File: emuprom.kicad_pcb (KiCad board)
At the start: 2 copper layers, 91.4 x 68.6 mm, 34 parts, among them J1 Conn_02x20_Odd_Even, J2 Conn_02x03_Odd_Even, J3 USB_C_Receptacle_USB2.0_14P, J4 Conn_01x02, U1 CY62256-70PC, U10 74HC244, U11 74HC04, U2 74HC244, U3 74HC244, U4 74HC245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

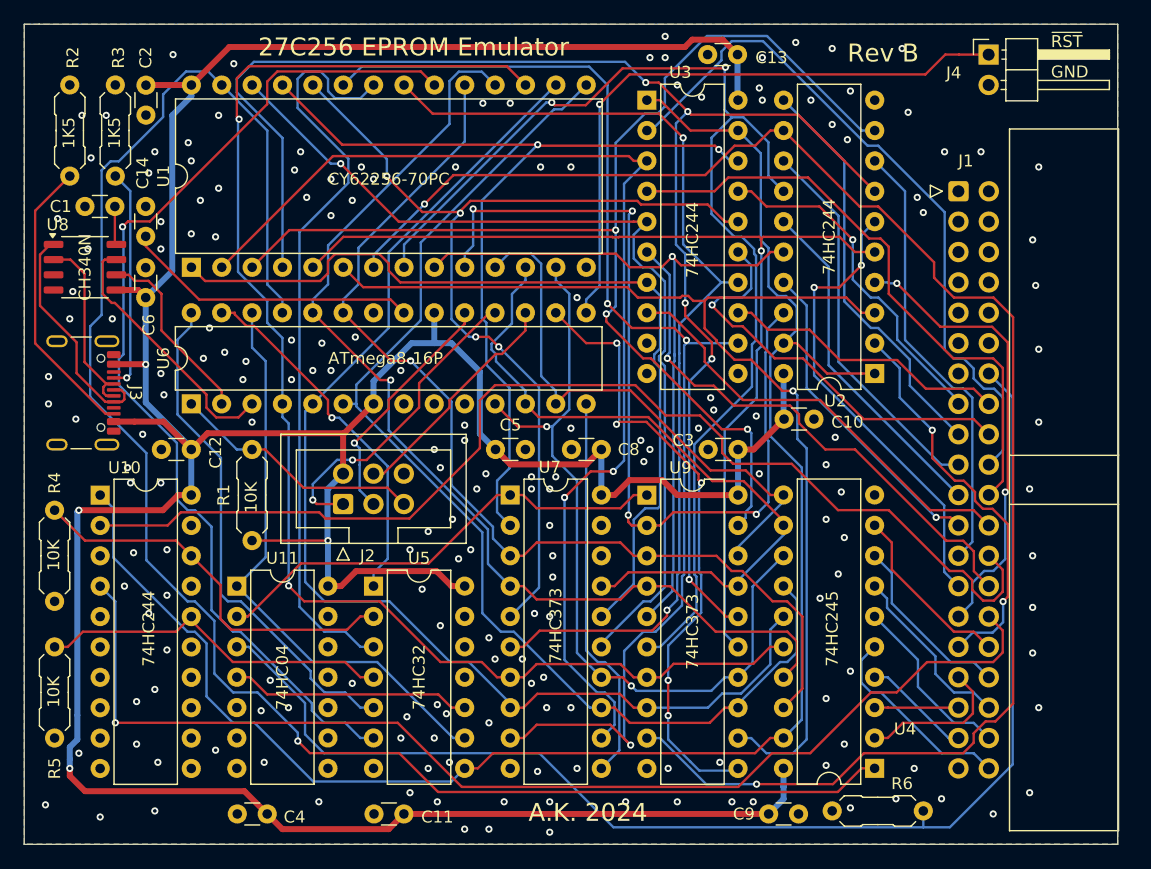
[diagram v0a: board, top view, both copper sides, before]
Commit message: Fix HW bug
U4 direction pin was tied to the wrong signal -
should be /RD instead of /WR. Tied it to the ground
instead. Now U4 74HC245 should be replaced with
74HC244, but it would require big layout change, so
I'm leaving it as is.
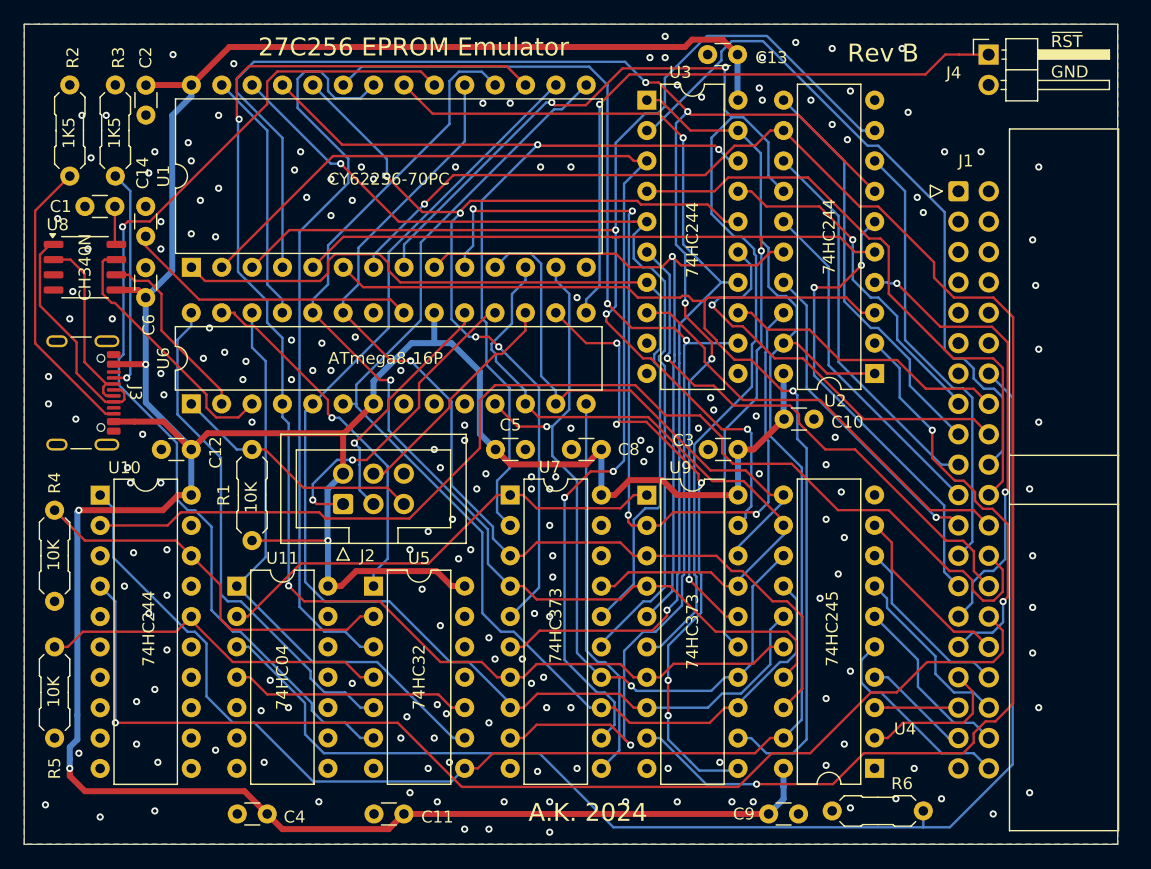
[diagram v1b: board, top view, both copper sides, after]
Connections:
- U4 pad 1: Net-(U1-~{WE}) -> GND
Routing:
- net Net-(U1-~{WE}): track 143.9 -> 21.1 mm, vias 1 -> 0
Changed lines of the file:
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@@
 			(layers "*.Cu" "*.Mask")
 			(remove_unused_layers no)
-			(net 80 "Net-(U1-~{WE})")
+			(net 1 "GND")
 			(pinfunction "A->B")
 			(pintype "input")
@@
 	)
 	(segment
-		(start 166.1309 125.725)
-		(end 173.5983 125.725)
-		(width 0.2)
-		(layer "F.Cu")
-		(net 80)
-	)
-	(segment
-		(start 210.2702 128.9731)
-		(end 212.2483 126.995)
-		(width 0.2)
-		(layer "F.Cu")
-		(net 80)
-	)
-	(segment
-		(start 165.1199 124.714)
-		(end 166.1309 125.725)
-		(width 0.2)
-		(layer "F.Cu")
-		(net 80)
-	)
-	(segment
-		(start 176.8464 128.9731)
-		(end 210.2702 128.9731)
-		(width 0.2)
-		(layer "F.Cu")
-		(net 80)
-	)
-	(segment
-		(start 212.2483 126.995)
-		(end 213.35 126.995)
-		(width 0.2)
-		(layer "F.Cu")
-		(net 80)
-	)
-	(segment
-		(start 173.5983 125.725)
-		(end 176.8464 128.9731)
-		(width 0.2)
-		(layer "F.Cu")
-		(net 80)
-	)
-	(via
-		(at 165.1199 124.714)
-		(size 0.6)
-		(drill 0.3)
-		(layers "F.Cu" "B.Cu")
-		(net 80)
-	)
-	(segment
-		(start 152.4542 100.63)
-		(end 147.7561 95.9319)
-		(width 0.2)
-		(layer "B.Cu")
-		(net 80)
-	)
-	(segment
-		(start 156.5168 113.035)
-		(end 155.8997 113.035)
-		(width 0.2)
-		(layer "B.Cu")
-		(net 80)
-	)
-	(segment
-		(start 149.4551 76.2376)
-		(end 150.1436 76.2376)
-		(width 0.2)
-		(layer "B.Cu")
-		(net 80)
-	)
-	(segment
-		(start 147.7561 95.9319)
-		(end 147.7561 90.0305)
-		(width 0.2)
-		(layer "B.Cu")
-		(net 80)
-	)
-	(segment
-		(start 148.7116 76.9811)
-		(end 149.4551 76.2376)
-		(width 0.2)
-		(layer "B.Cu")
-		(net 80)
-	)
-	(segment
-		(start 153.8556 72.5256)
-		(end 153.8556 70.641)
-		(width 0.2)
-		(layer "B.Cu")
-		(net 80)
-	)
-	(segment
-		(start 165.1199 124.714)
-		(end 165.1199 124.0157)
-		(width 0.2)
-		(layer "B.Cu")
-		(net 80)
-	)
-	(segment
 		(start 163.83 87.7983)
 		(end 162.57 86.5383)
@@
 	)
 	(segment
-		(start 148.7116 89.075)
-		(end 148.7116 76.9811)
-		(width 0.2)
-		(layer "B.Cu")
-		(net 80)
-	)
-	(segment
-		(start 165.1199 124.0157)
-		(end 161.7492 120.645)
-		(width 0.2)
-		(layer "B.Cu")
-		(net 80)
-	)
-	(segment
-		(start 161.7492 120.645)
-		(end 159.7104 120.645)
-		(width 0.2)
-		(layer "B.Cu")
-		(net 80)
-	)
-	(segment
-		(start 155.7667 68.7299)
-		(end 157.6349 68.7299)
-		(width 0.2)
-		(layer "B.Cu")
-		(net 80)
-	)
-	(segment
-		(start 159.7104 120.645)
-		(end 158.1431 119.0777)
-		(width 0.2)
-		(layer "B.Cu")
-		(net 80)
-	)
-	(segment
-		(start 153.8556 70.641)
-		(end 155.7667 68.7299)
-		(width 0.2)
-		(layer "B.Cu")
-		(net 80)
-	)
-	(segment
 		(start 162.57 73.665)
 		(end 158.76 69.855)
@@
 		(width 0.2)
 		(layer "B.Cu")
-		(net 80)
-	)
-	(segment
-		(start 155.8997 113.035)
-		(end 152.4542 109.5895)
-		(width 0.2)
-		(layer "B.Cu")
-		(net 80)
-	)
-	(segment
-		(start 147.7561 90.0305)
-		(end 148.7116 89.075)
-		(width 0.2)
-		(layer "B.Cu")
-		(net 80)
-	)
-	(segment
-		(start 157.6349 68.7299)
-		(end 158.76 69.855)
-		(width 0.2)
-		(layer "B.Cu")
-		(net 80)
-	)
-	(segment
-		(start 152.4542 109.5895)
-		(end 152.4542 100.63)
-		(width 0.2)
-		(layer "B.Cu")
-		(net 80)
-	)
-	(segment
-		(start 158.1431 119.0777)
-		(end 158.1431 114.6613)
-		(width 0.2)
-		(layer "B.Cu")
-		(net 80)
-	)
-	(segment
-		(start 158.1431 114.6613)
-		(end 156.5168 113.035)
-		(width 0.2)
-		(layer "B.Cu")
-		(net 80)
-	)
-	(segment
-		(start 150.1436 76.2376)
-		(end 153.8556 72.5256)
-		(width 0.2)
-		(layer "B.Cu")

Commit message: Revision C: redesign to fix U4 problem
Reduced PCB footprint slightly, change U11 74HC04 -> 74HC02
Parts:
- U11: value 74HC04 -> 74HC02
- U4: value 74HC245 -> 74HC244
- moved C9 5.08 mm to (199.4, 130.8)
- moved R6 4.06 mm to (205.7, 130.6)
- moved J1 3.19 mm to (217.2, 78.7)
- moved J4 2.47 mm to (220.4, 67.3)
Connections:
- U11 pad 1: Net-(U6-PC3) -> Net-(U11-Pad1)
- U11 pad 10: unconnected-(U11-Pad10) -> Net-(U11-Pad10)
- U11 pad 11: GND -> Net-(U11-Pad10)
- U11 pad 12: unconnected-(U11-Pad12) -> Net-(U11-Pad10)
- U11 pad 13: GND -> Net-(U11-Pad13)
- U11 pad 2: Net-(U7-OE) -> Net-(J1-Pin_14)
- U11 pad 4: Net-(U11-Pad4) -> Net-(U7-OE)
- U11 pad 5: GND -> Net-(U6-PC3)
- U11 pad 6: unconnected-(U11-Pad6) -> Net-(U6-PC3)
- U11 pad 8: unconnected-(U11-Pad8) -> Net-(U1-~{OE})
- U11 pad 9: GND -> Net-(U1-~{CS})
- U4 pad 1: GND -> Net-(U4-1OE)
- U4 pad 11: /RAMD7 -> /D7
- U4 pad 12: /RAMD6 -> /RAMD3
- U4 pad 13: /RAMD5 -> /D6
- U4 pad 14: /RAMD4 -> /RAMD2
- U4 pad 15: /RAMD3 -> /D5
- U4 pad 16: /RAMD2 -> /RAMD1
- U4 pad 17: /RAMD1 -> /D4
- U4 pad 19: Net-(U10-1OE) -> Net-(U4-1OE)
- U4 pad 3: /D1 -> /RAMD4
- U4 pad 4: /D2 -> /D1
- U4 pad 5: /D3 -> /RAMD5
- U4 pad 6: /D4 -> /D2
- U4 pad 7: /D5 -> /RAMD6
- U4 pad 8: /D6 -> /D3
- U4 pad 9: /D7 -> /RAMD7
- U5 pad 10: Net-(U11-Pad4) -> Net-(U11-Pad1)
- U5 pad 11: unconnected-(U5-Pad11) -> Net-(U4-1OE)
- U5 pad 12: GND -> Net-(U10-1OE)
- U5 pad 13: GND -> Net-(U11-Pad13)
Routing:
- net VCC: track 314.0 -> 261.6 mm, vias 4 -> 3
- net Net-(U4-1OE): track 0.00 -> 38.9 mm
- net /RAMA6: track 122.8 -> 161.2 mm, vias 5 -> 4
- net Net-(U1-~{OE}): track 63.8 -> 98.8 mm, vias 0 -> 2
- net Net-(U10-1OE): track 146.8 -> 179.5 mm, vias 0 -> 1
- net /RAMA2: track 99.6 -> 73.1 mm
- net Net-(U11-Pad1): track 0.00 -> 23.3 mm
- net Net-(J1-Pin_26): track 95.6 -> 74.2 mm, vias 0 -> 1
- net /RAMA12: track 94.4 -> 115.3 mm
- net Net-(U1-~{CS}): track 87.2 -> 107.9 mm, vias 1 -> 3
- net Net-(U11-Pad4): track 20.1 -> 0.00 mm
- net Net-(U7-OE): track 39.4 -> 58.4 mm, vias 0 -> 1
- net /RAMA5: track 84.6 -> 102.4 mm
- net Net-(U6-PC3): track 48.6 -> 65.1 mm, vias 0 -> 1
- net /RAMA0: track 74.1 -> 58.1 mm, vias 4 -> 3
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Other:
- board size 91.4 x 68.6 mm -> 88.3 x 68.6 mm
- board text added: "Rev C"
- board text removed: "Rev B"

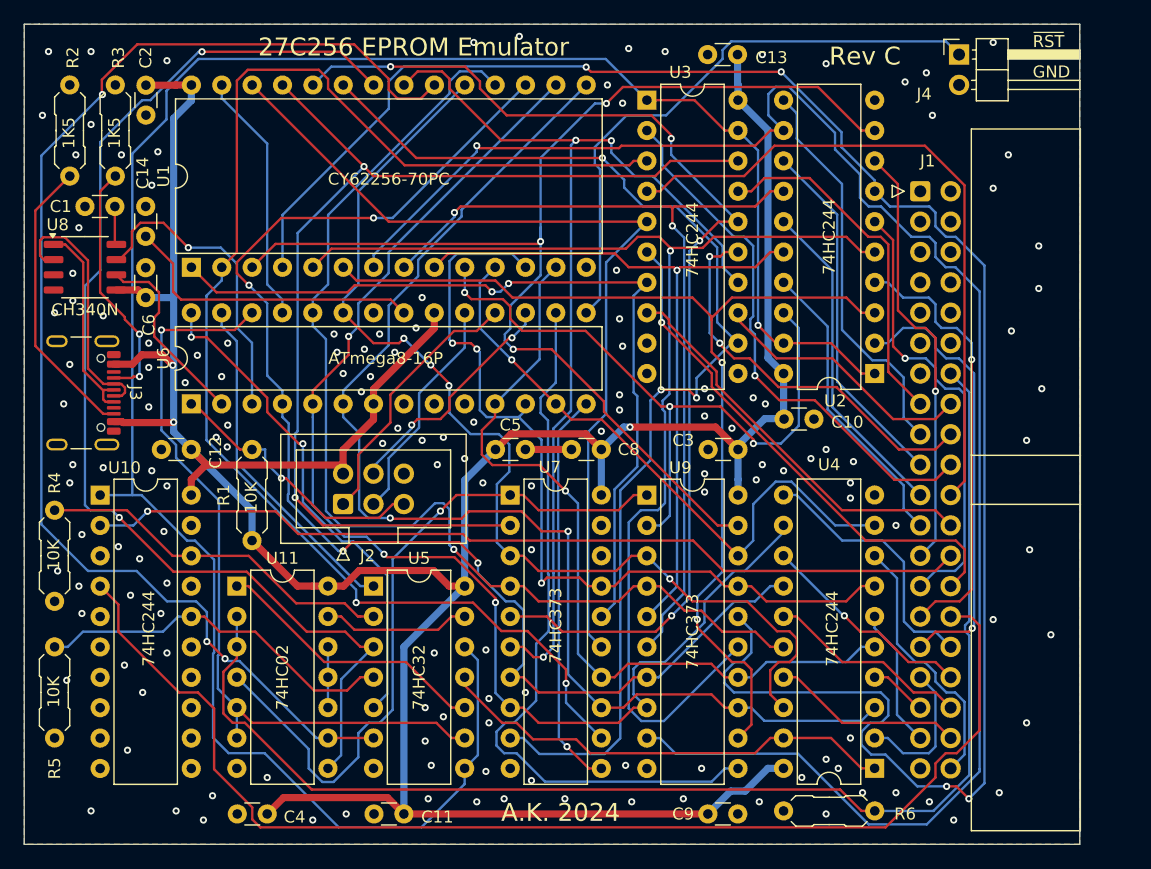
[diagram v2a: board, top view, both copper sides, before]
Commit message: rev D: Fix U4 output being swapped with input
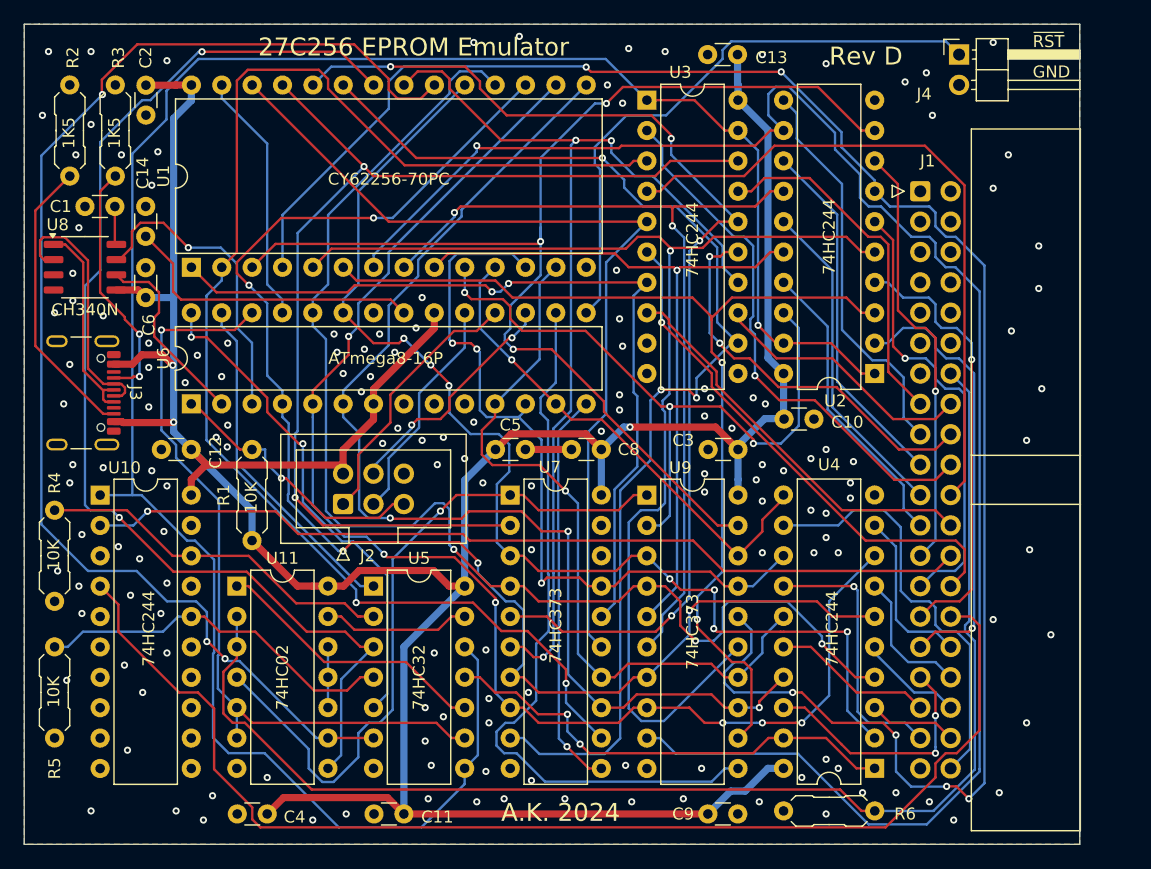
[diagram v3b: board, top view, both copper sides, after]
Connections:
- U4 pad 11: /D7 -> /RAMD7
- U4 pad 12: /RAMD3 -> /D3
- U4 pad 13: /D6 -> /RAMD6
- U4 pad 14: /RAMD2 -> /D2
- U4 pad 15: /D5 -> /RAMD5
- U4 pad 16: /RAMD1 -> /D1
- U4 pad 17: /D4 -> /RAMD4
- U4 pad 18: /RAMD0 -> /D0
- U4 pad 2: /D0 -> /RAMD0
- U4 pad 3: /RAMD4 -> /D4
- U4 pad 4: /D1 -> /RAMD1
- U4 pad 5: /RAMD5 -> /D5
- U4 pad 6: /D2 -> /RAMD2
- U4 pad 7: /RAMD6 -> /D6
- U4 pad 8: /D3 -> /RAMD3
- U4 pad 9: /RAMD7 -> /D7
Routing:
- net /RAMD1: track 93.1 -> 107.2 mm, vias 1 -> 3
- net /D3: track 22.3 -> 35.8 mm
- net /D2: track 11.7 -> 22.7 mm, vias 0 -> 1
- net /RAMD7: track 52.4 -> 41.8 mm
- net /D0: track 12.2 -> 21.2 mm, vias 0 -> 2
- net /RAMD2: track 109.9 -> 118.7 mm, vias 4 -> 5
- net /D4: track 16.1 -> 7.41 mm
- net /D1: track 4.87 -> 13.5 mm
- net /D5: track 17.1 -> 8.76 mm
- net /RAMD0: track 89.3 -> 97.4 mm, vias 4 -> 7
- net /D7: track 22.2 -> 14.1 mm
- net /RAMD6: track 71.4 -> 63.8 mm
- net /RAMD3: track 106.8 -> 114.2 mm, vias 3 -> 6
- net /RAMD4: track 103.8 -> 96.6 mm, vias 2 -> 3
- net /D6: track 18.2 -> 11.6 mm, vias 1 -> 0
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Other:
- board text added: "Rev D"
- board text removed: "Rev C"
